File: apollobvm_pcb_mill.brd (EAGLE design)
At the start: 98 x 60 mm, 25 parts

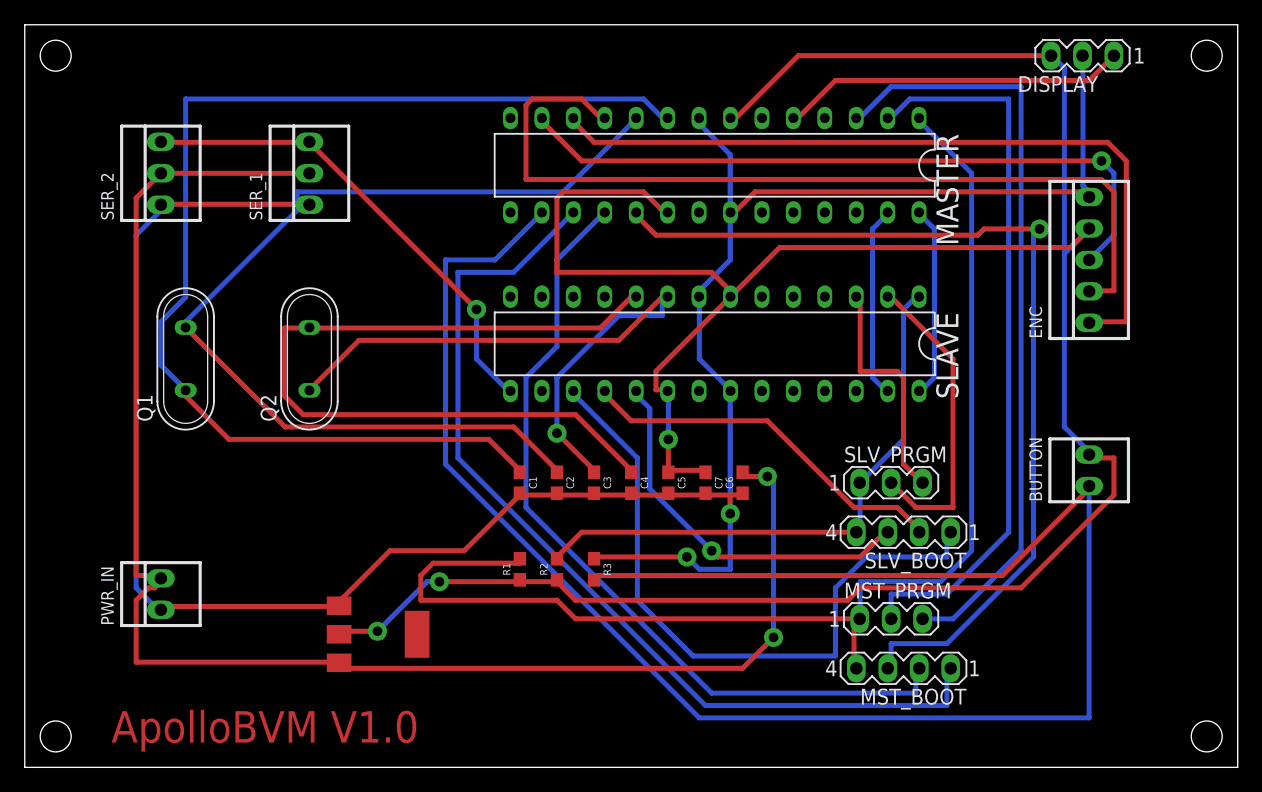
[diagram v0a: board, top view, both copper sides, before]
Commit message: Added millable version
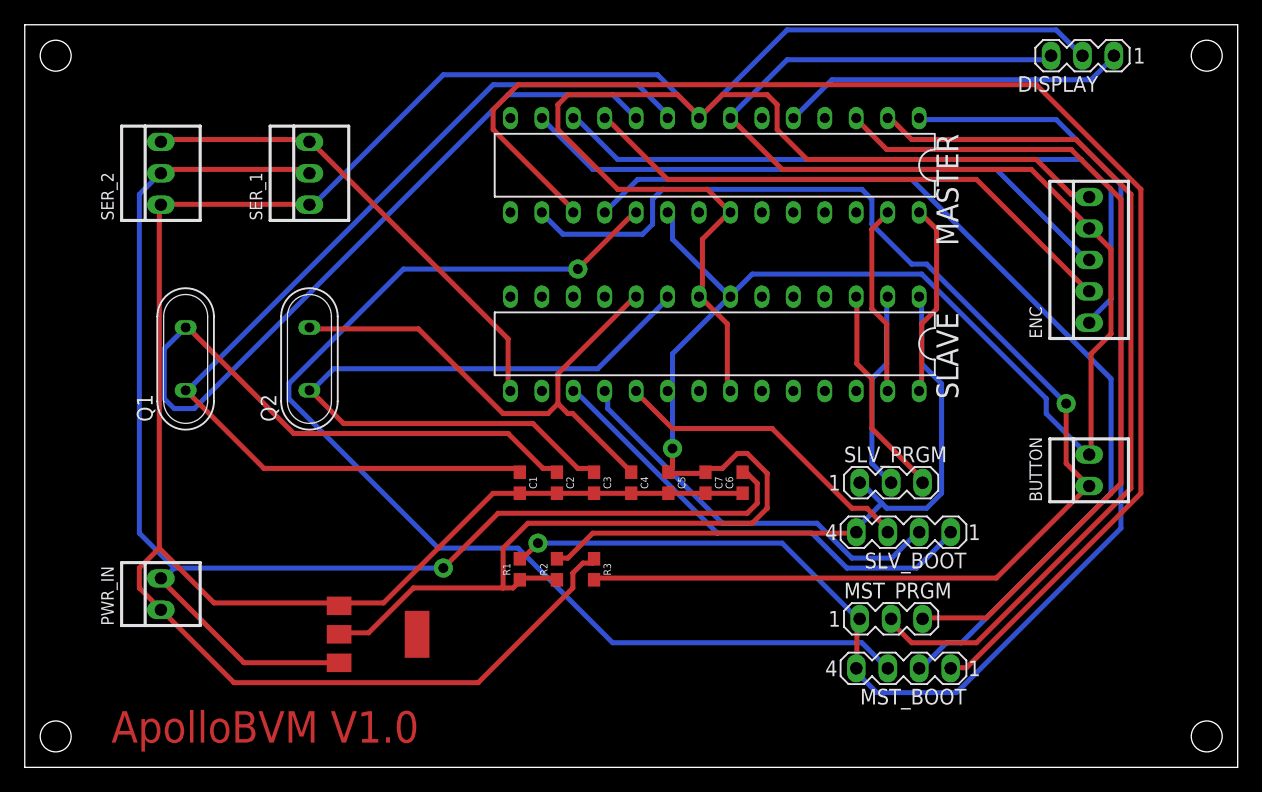
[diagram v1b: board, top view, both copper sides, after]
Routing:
- net GND: track 193.5 -> 298.4 mm, vias 2 -> 0
- net N$14: track 148.6 -> 104.7 mm, vias 0 -> 1
- net N$18: track 77.4 -> 113.4 mm
- net N$10: track 71.1 -> 44.9 mm
- net N$4: track 65.6 -> 42.8 mm
- net +5V: track 221.4 -> 200.4 mm, vias 3 -> 1
- net N$15: track 54.7 -> 37.7 mm
- net N$20: track 77.1 -> 92.4 mm
- net N$5: track 94.9 -> 80.2 mm
- net N$19: track 66.5 -> 79.3 mm
- net N$24: track 59.0 -> 71.4 mm
- net N$6: track 79.5 -> 91.0 mm
- net N$22: track 25.2 -> 16.2 mm
- net N$1: track 100.8 -> 108.7 mm, vias 0 -> 1
- net N$9: track 56.0 -> 49.0 mm, vias 1 -> 0
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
